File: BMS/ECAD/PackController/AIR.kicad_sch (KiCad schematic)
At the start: 33 parts, among them J1 Conn_01x08, K401 AIR_P, K402 AIR_N, Q3 BC846, Q4 BC846, Q402 DMP4065S-7, Q404 DMP4065S-7, U401 ADCMP393ARUZ

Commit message: schematic finished, review tbd
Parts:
- R416, R420: value 4k7R -> 1kR
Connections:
- net DANGER_V: now reaches Q3.1 (B), R416.1
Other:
- moved on the sheet: C401, Q3, Q4, Q402, Q404, R409, R410, R411, R412, R413, R414, R415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

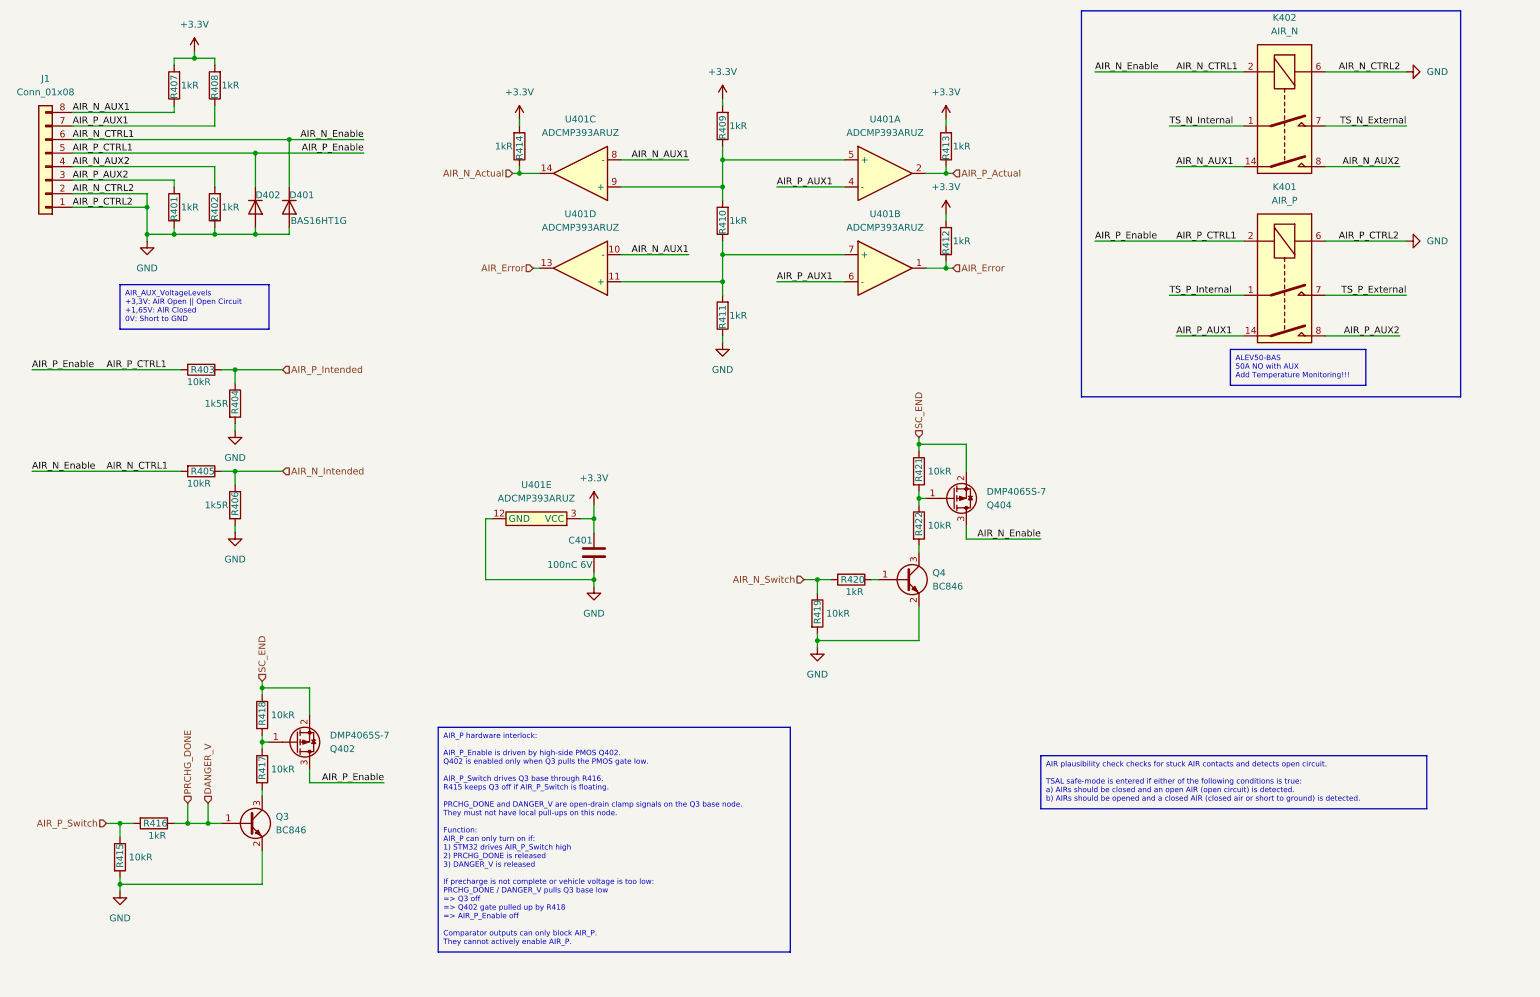
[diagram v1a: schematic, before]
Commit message: close to finish BMS master, only some footprints needed
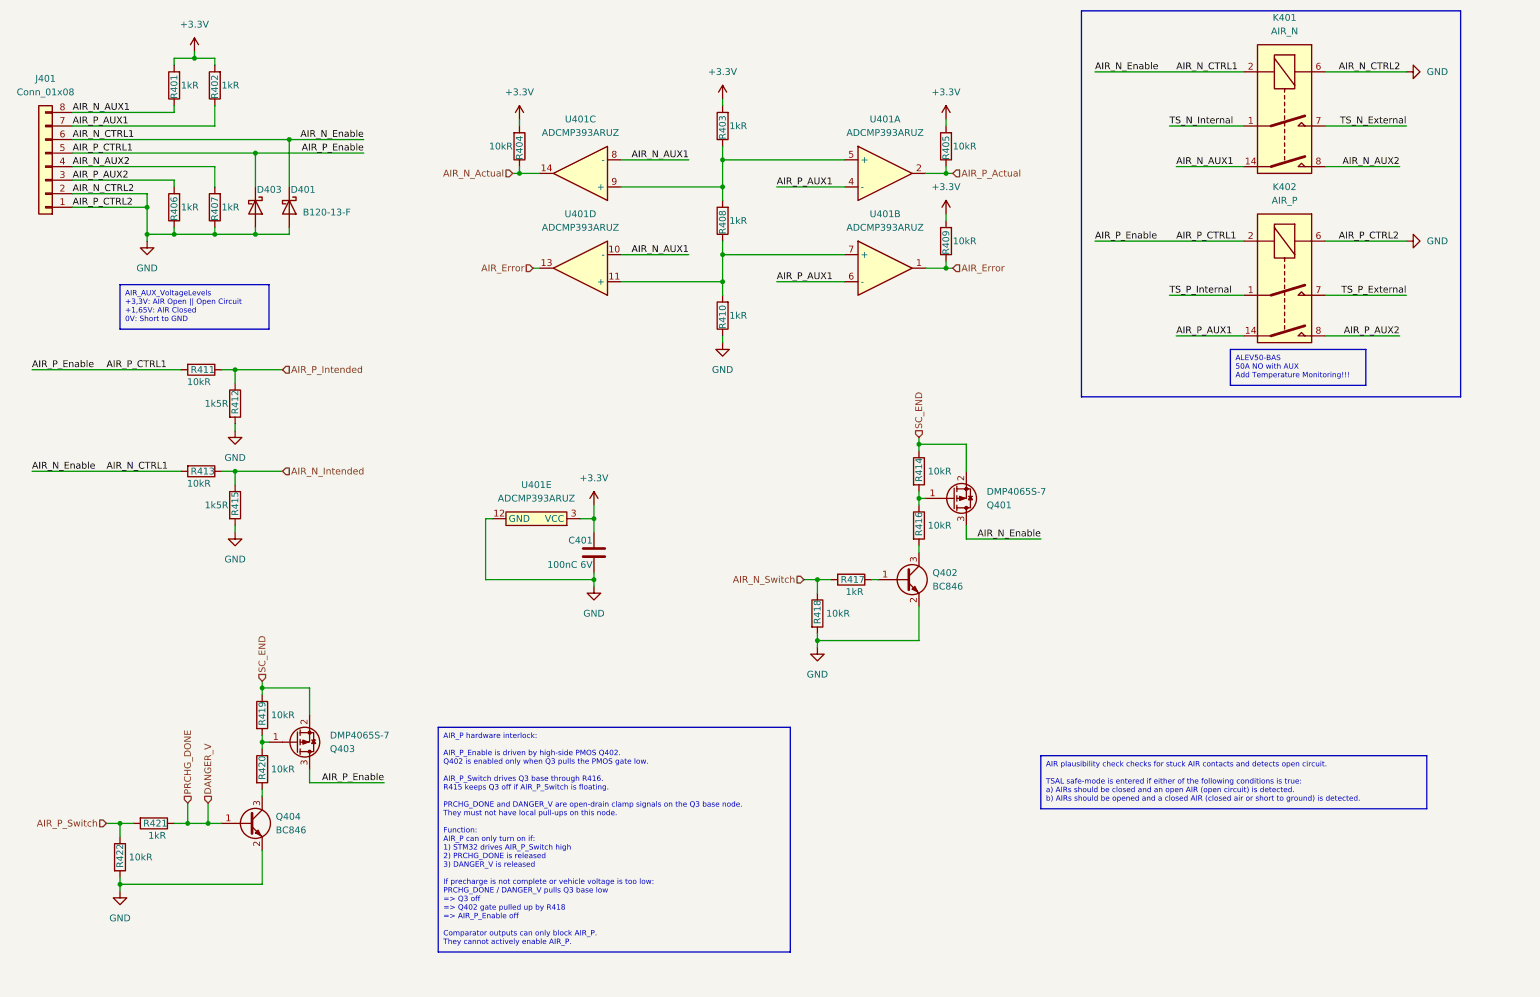
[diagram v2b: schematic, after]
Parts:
- removed D401, D402: BAS16HT1G, Diode_SMD:D_SOD-323F, symbol Device:D
- added D401, D403: B120-13-F, Diode_SMD:D_SMA, symbol Diode:B120-E3
- K401: renamed from K402; now left out of the parts list
- K402: renamed from K401; now left out of the parts list
- R404: renamed from R414; value 1kR -> 10kR
- R405: renamed from R413; value 1kR -> 10kR
- R409: renamed from R412; value 1kR -> 10kR
- U401: footprint (none) -> Package_SO:TSSOP-14_4.4x5mm_P0.65mm
- renumbered J1 to J401, Q404 to Q401, Q4 to Q402, Q402 to Q403, Q3 to Q404, R407 to R401, R408 to R402, R409 to R403, R401 to R406, R402 to R407, R410 to R408, R411 to R410, R403 to R411, R404 to R412, R405 to R413, R421 to R414, R406 to R415, R422 to R416, R420 to R417, R419 to R418, R418 to R419, R417 to R420, R416 to R421, R415 to R422
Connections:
- net AIR_N_CTRL1: now also D401.1 (K)
- net AIR_P_CTRL1: now also D403.1 (K)
- net GND: now also D401.2 (A), D403.2 (A)

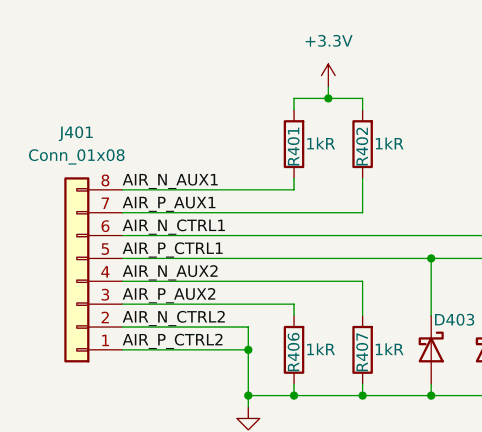
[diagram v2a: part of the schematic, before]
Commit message: Add several auxilary circuits to BMS Master
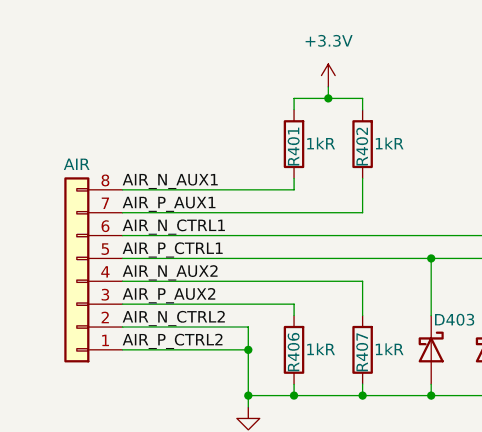
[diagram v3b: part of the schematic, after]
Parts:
- AIR: renamed from J401; value Conn_01x08 -> (none); footprint (none) -> Connector_Molex:Molex_Micro-Fit_3.0_43045-0812_2x04_P3.00mm_Vertical
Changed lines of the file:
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@@
 		(in_pos_files yes)
 		(dnp no)
-		(fields_autoplaced yes)
-		(property "Reference" "J401"
-			(at 19.05 25.4 0)
+		(property "Reference" "AIR"
+			(at 19.05 28.956 0)
 			(show_name no)
 			(do_not_autoplace no)
@@
 			)
 		)
-		(property "Value" "Conn_01x08"
+		(property "Value" ""
 			(at 19.05 27.94 0)
 			(show_name no)
@@
 			)
 		)
-		(property "Footprint" ""
+		(property "Footprint" "Connector_Molex:Molex_Micro-Fit_3.0_43045-0812_2x04_P3.00mm_Vertical"
 			(at 19.05 41.91 0)
 			(hide yes)
@@
 			(project "Pack_Controller"
 				(path "/58a1c93e-baba-4d23-9191-955e00968735/9e3af51c-36cf-42ea-bd79-21f3fecec64c"
-					(reference "J401")
+					(reference "AIR")
 					(unit 1)
 				)

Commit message: finalised schematic of pack controller
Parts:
- D401, D403: value B120-13-F -> B140-13-F
- R411, R413: value 10kR -> 39kR
- R412, R415: value 1k5R -> 10kR
- U401: value ADCMP393ARUZ -> ADCMP393ARZ; footprint Package_SO:TSSOP-14_4.4x5mm_P0.65mm -> Package_SO:SOIC-14_3.9x8.7mm_P1.27mm
- renumbered AIR to AIR401
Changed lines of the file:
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@@
 			)
 		)
-		(property "Value" "ADCMP393ARUZ"
+		(property "Value" "ADCMP393ARZ"
 			(at 176.53 35.56 0)
 			(show_name no)
@@
 			)
 		)
-		(property "Footprint" "Package_SO:TSSOP-14_4.4x5mm_P0.65mm"
+		(property "Footprint" "Package_SO:SOIC-14_3.9x8.7mm_P1.27mm"
 			(at 171.45 38.1 0)
 			(hide yes)
@@
 			)
 		)
-		(property "Value" "ADCMP393ARUZ"
+		(property "Value" "ADCMP393ARZ"
 			(at 119.38 53.34 0)
 			(show_name no)
@@
 			)
 		)
-		(property "Footprint" "Package_SO:TSSOP-14_4.4x5mm_P0.65mm"
+		(property "Footprint" "Package_SO:SOIC-14_3.9x8.7mm_P1.27mm"
 			(at 124.46 66.04 0)
 			(hide yes)
@@
 			)
 		)
-		(property "Value" "10kR"
+		(property "Value" "39kR"
 			(at 50.038 82.296 90)
 			(show_name no)
@@
 			)
 		)
-		(property "Value" "B120-13-F"
+		(property "Value" "B140-13-F"
 			(at 67.31 50.4824 90)
 			(show_name no)
@@
 			)
 		)
-		(property "Value" "10kR"
+		(property "Value" "39kR"
 			(at 50.038 101.346 90)
 			(show_name no)
@@
 			)
 		)
-		(property "Value" "ADCMP393ARUZ"
+		(property "Value" "ADCMP393ARZ"
 			(at 119.38 35.56 0)
 			(show_name no)
@@
 			)
 		)
-		(property "Footprint" "Package_SO:TSSOP-14_4.4x5mm_P0.65mm"
+		(property "Footprint" "Package_SO:SOIC-14_3.9x8.7mm_P1.27mm"
 			(at 124.46 48.26 0)
 			(hide yes)
@@
 			)
 		)
-		(property "Value" "1k5R"
+		(property "Value" "10kR"
 			(at 53.34 86.36 0)
 			(show_name no)
@@
 			)
 		)
-		(property "Value" "1k5R"
+		(property "Value" "10kR"
 			(at 53.34 105.41 0)
 			(show_name no)
@@
 			)
 		)
-		(property "Value" "B120-13-F"
+		(property "Value" "B140-13-F"
 			(at 60.96 50.4824 90)
 			(hide yes)
@@
 		(in_pos_files yes)
 		(dnp no)
-		(property "Reference" "AIR"
+		(property "Reference" "AIR401"
 			(at 19.05 28.956 0)
 			(show_name no)
@@
 			(project "Pack_Controller"
 				(path "/58a1c93e-baba-4d23-9191-955e00968735/9e3af51c-36cf-42ea-bd79-21f3fecec64c"
-					(reference "AIR")
+					(reference "AIR401")
 					(unit 1)
 				)
@@
 			)
 		)
-		(property "Value" "ADCMP393ARUZ"
+		(property "Value" "ADCMP393ARZ"
 			(at 111.125 104.14 0)
 			(show_name no)
@@
 			)
 		)
-		(property "Footprint" "Package_SO:TSSOP-14_4.4x5mm_P0.65mm"
+		(property "Footprint" "Package_SO:SOIC-14_3.9x8.7mm_P1.27mm"
 			(at 116.84 111.76 0)
 			(hide yes)
@@
 			)
 		)
-		(property "Value" "ADCMP393ARUZ"
+		(property "Value" "ADCMP393ARZ"
 			(at 176.53 53.34 0)
 			(show_name no)
@@
 			)
 		)
-		(property "Footprint" "Package_SO:TSSOP-14_4.4x5mm_P0.65mm"
+		(property "Footprint" "Package_SO:SOIC-14_3.9x8.7mm_P1.27mm"
 			(at 171.45 55.88 0)
 			(hide yes)
